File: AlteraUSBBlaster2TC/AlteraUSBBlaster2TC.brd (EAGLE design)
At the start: 39.4 x 34 mm, 13 parts, among them U1 NCP1117LPST33T3G

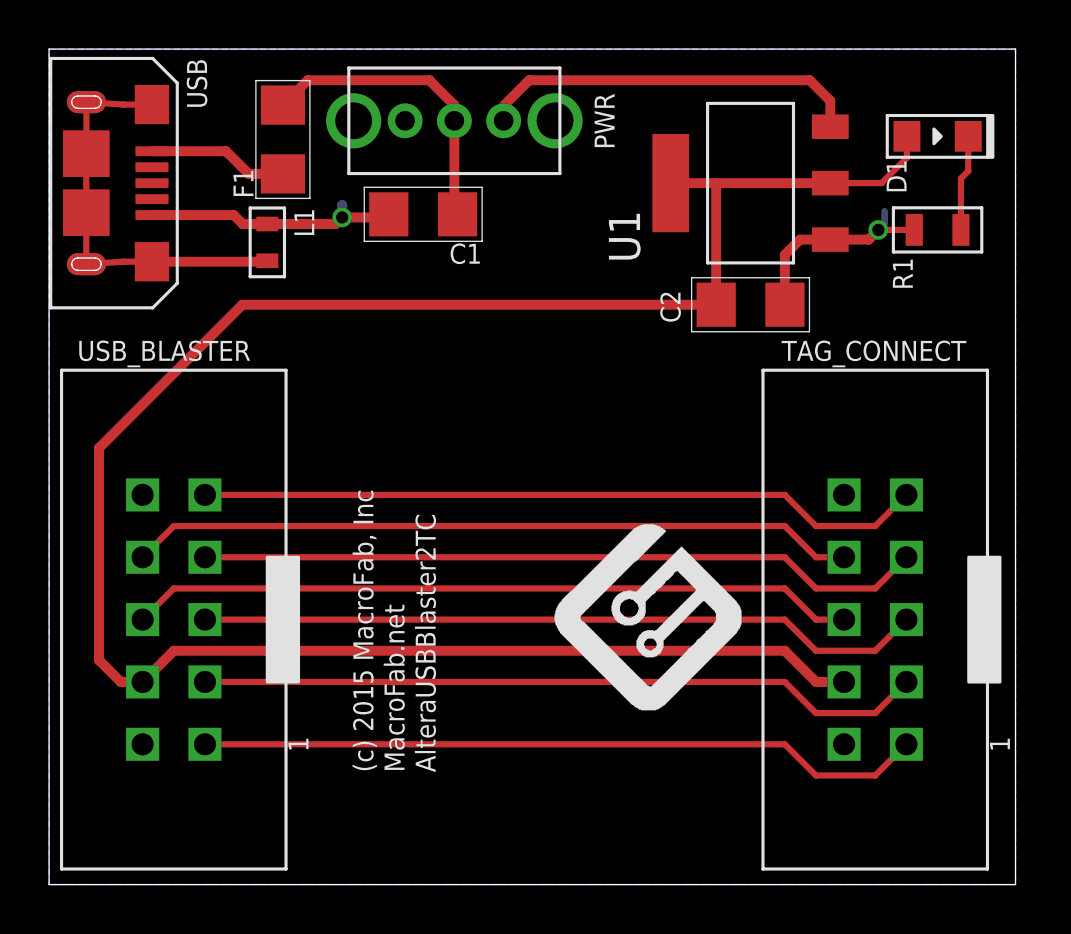
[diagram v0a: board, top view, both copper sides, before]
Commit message: Added AVRISP2TC
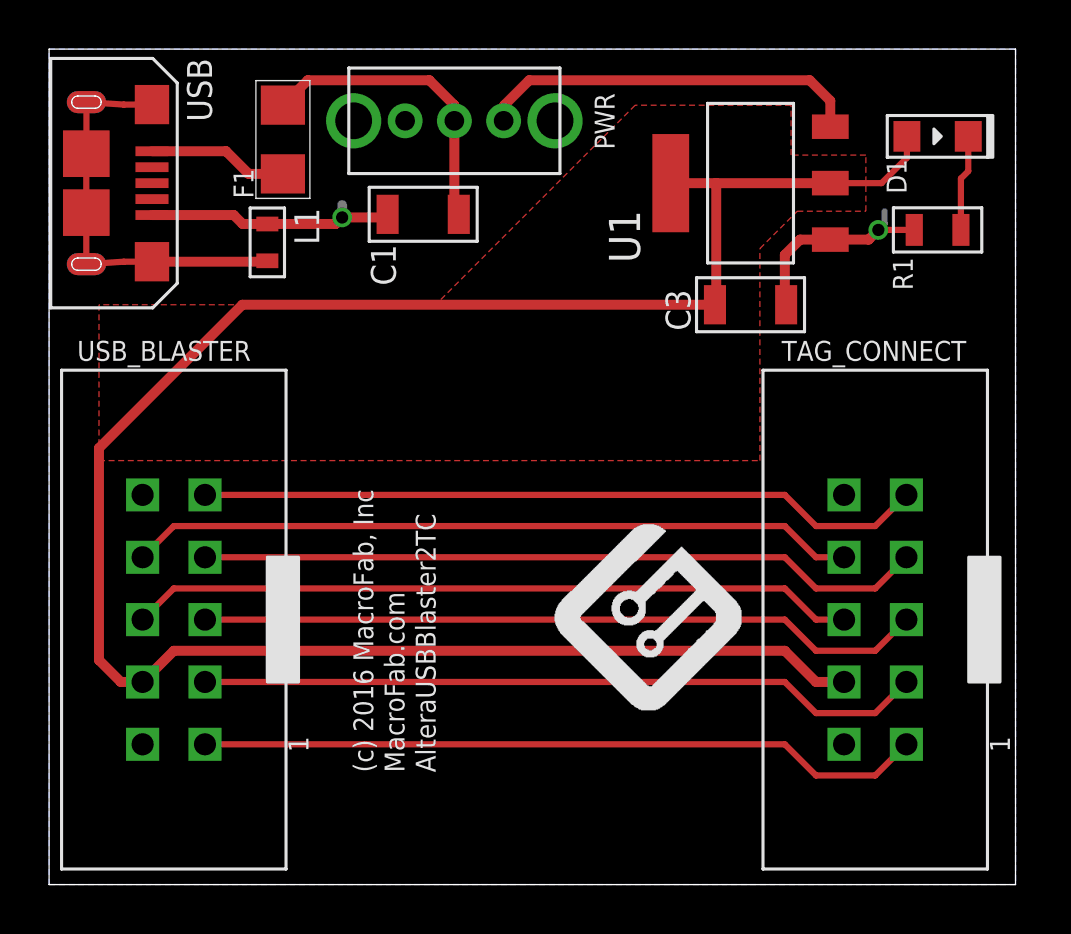
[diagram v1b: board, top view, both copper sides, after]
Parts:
- removed C2: 10uF, PP_Passives:1206
- added C3: 10uF, MF_Passives:C1206
- C1: device PP_Passives:1206 -> MF_Passives:C1206
- D1: value MF-LED-0603-RED -> MF-LED-0805-RED
- FRAME1: value MF_FRAMEDEFAULT -> (none)
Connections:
- net GND: now also C1.P$2, C3.P$2; no longer C1.2, C2.2
- net N$2: now also C1.P$1; no longer C1.1
- net VCC: now also C3.P$1; no longer C2.1
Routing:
- added copper zone on layer 1, net VCC
